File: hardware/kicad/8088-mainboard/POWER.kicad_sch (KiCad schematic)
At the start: 4 parts, among them J2 POWER 5v

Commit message: Add PSB board design
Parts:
- renumbered J2 to J1
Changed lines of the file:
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@@
 		(dnp no)
 		(fields_autoplaced yes)
-		(property "Reference" "J2"
+		(property "Reference" "J1"
 			(at 105.41 82.5499 90)
 			(show_name no)
@@
 			(project "8088-mainboard"
 				(path "/15ce4f45-6f32-456e-874c-aac11293789a/e9d836d6-3c3a-4b6e-a562-389c64894272"
-					(reference "J2")
+					(reference "J1")
 					(unit 1)
 				)

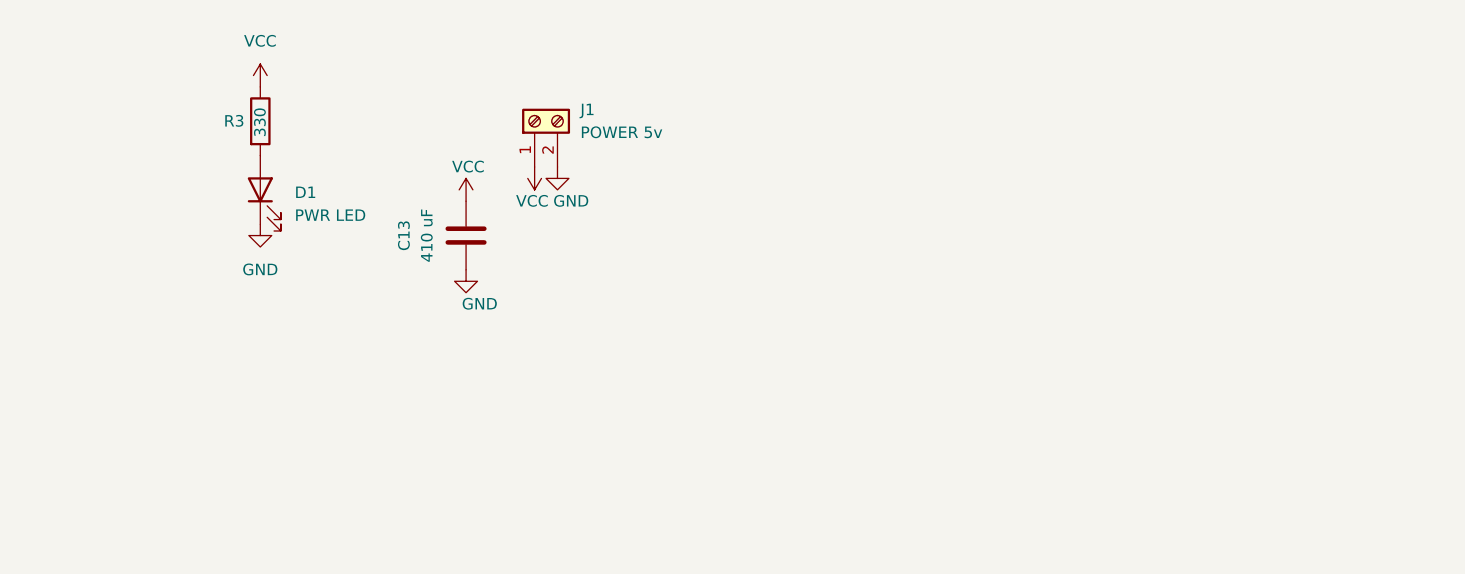
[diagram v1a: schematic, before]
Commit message: Update 8088-mainboard schematics for refined connections and label adjustments
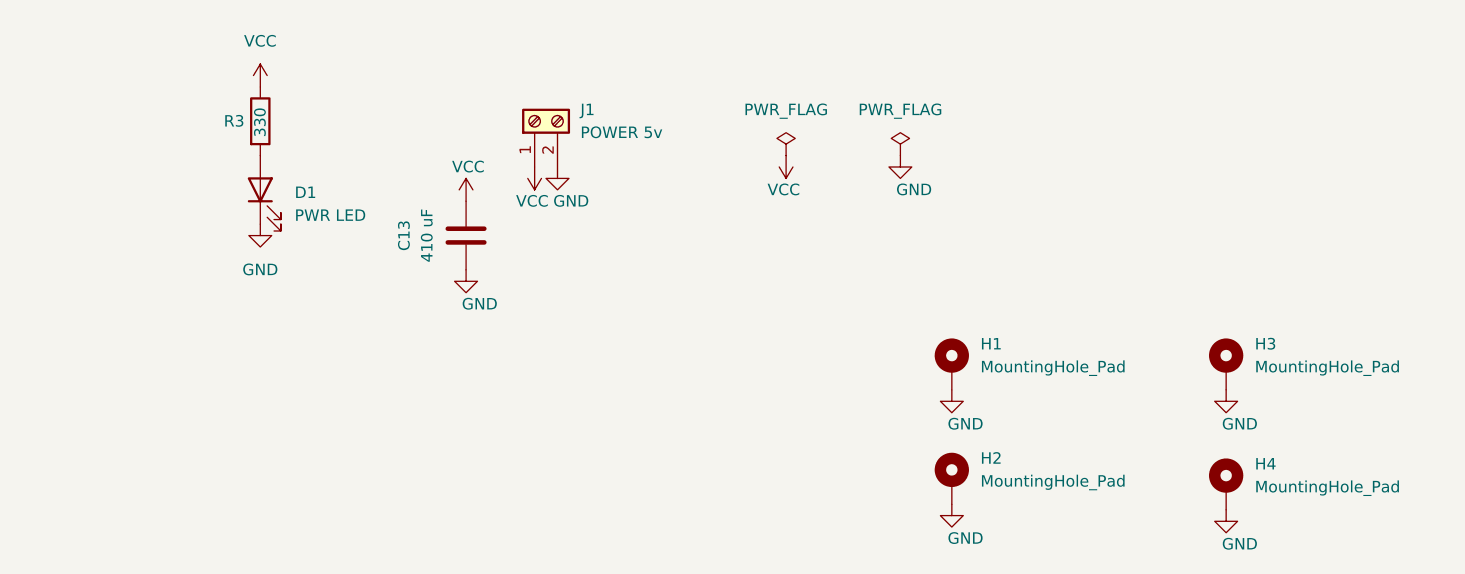
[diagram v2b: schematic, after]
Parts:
- added H1, H2, H3, H4: MountingHole_Pad, MountingHole:MountingHole_3.2mm_M3_Pad, symbol Mechanical:MountingHole_Pad
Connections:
- net GND: now also H1.1, H2.1, H3.1, H4.1

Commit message: Update 8086-mainboard scheme
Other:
- moved on the sheet: H1, H2, H3, H4
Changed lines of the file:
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@@
 	(symbol
 		(lib_id "power:GND")
-		(at 146.685 126.365 0)
+		(at 147.32 127 0)
 		(unit 1)
 		(body_style 1)
@@
 		(dnp no)
 		(property "Reference" "#PWR094"
-			(at 146.685 132.715 0)
+			(at 147.32 133.35 0)
 			(hide yes)
 			(show_name no)
@@
 		)
 		(property "Value" "GND"
-			(at 148.209 130.175 0)
+			(at 148.844 130.81 0)
 			(show_name no)
 			(do_not_autoplace no)
@@
 		)
 		(property "Footprint" ""
-			(at 146.685 126.365 0)
-			(hide yes)
-			(show_name no)
-			(do_not_autoplace no)
-			(effects
-				(font
-					(size 1.27 1.27)
-				)
-			)
-		)
-		(property "Datasheet" ""
-			(at 146.685 126.365 0)
+			(at 147.32 127 0)
+			(hide yes)
+			(show_name no)
+			(do_not_autoplace no)
+			(effects
+				(font
+					(size 1.27 1.27)
+				)
+			)
+		)
+		(property "Datasheet" ""
+			(at 147.32 127 0)
 			(hide yes)
 			(show_name no)
@@
 		)
 		(property "Description" "Power symbol creates a global label with name \"GND\" , ground"
-			(at 146.685 126.365 0)
+			(at 147.32 127 0)
 			(hide yes)
 			(show_name no)
@@
 	(symbol
 		(lib_id "Mechanical:MountingHole_Pad")
-		(at 146.685 111.125 0)
+		(at 147.32 111.76 0)
 		(unit 1)
 		(body_style 1)
@@
 		(fields_autoplaced yes)
 		(property "Reference" "H1"
-			(at 149.86 108.5849 0)
+			(at 150.495 109.2199 0)
 			(show_name no)
 			(do_not_autoplace no)
@@
 		)
 		(property "Value" "MountingHole_Pad"
-			(at 149.86 111.1249 0)
+			(at 150.495 111.7599 0)
 			(show_name no)
 			(do_not_autoplace no)
@@
 		)
 		(property "Footprint" "MountingHole:MountingHole_3.2mm_M3_Pad"
-			(at 146.685 111.125 0)
-			(hide yes)
-			(show_name no)
-			(do_not_autoplace no)
-			(effects
-				(font
-					(size 1.27 1.27)
-				)
-			)
-		)
-		(property "Datasheet" ""
-			(at 146.685 111.125 0)
+			(at 147.32 111.76 0)
+			(hide yes)
+			(show_name no)
+			(do_not_autoplace no)
+			(effects
+				(font
+					(size 1.27 1.27)
+				)
+			)
+		)
+		(property "Datasheet" ""
+			(at 147.32 111.76 0)
 			(hide yes)
 			(show_name no)
@@
 		)
 		(property "Description" "Mounting Hole with connection"
-			(at 146.685 111.125 0)
+			(at 147.32 111.76 0)
 			(hide yes)
 			(show_name no)
@@
 	(symbol
 		(lib_id "power:GND")
-		(at 146.685 113.665 0)
+		(at 147.32 114.3 0)
 		(unit 1)
 		(body_style 1)
@@
 		(dnp no)
 		(property "Reference" "#PWR093"
-			(at 146.685 120.015 0)
+			(at 147.32 120.65 0)
 			(hide yes)
 			(show_name no)
@@
 		)
 		(property "Value" "GND"
-			(at 148.209 117.475 0)
+			(at 148.844 118.11 0)
 			(show_name no)
 			(do_not_autoplace no)
@@
 		)
 		(property "Footprint" ""
-			(at 146.685 113.665 0)
-			(hide yes)
-			(show_name no)
-			(do_not_autoplace no)
-			(effects
-				(font
-					(size 1.27 1.27)
-				)
-			)
-		)
-		(property "Datasheet" ""
-			(at 146.685 113.665 0)
+			(at 147.32 114.3 0)
+			(hide yes)
+			(show_name no)
+			(do_not_autoplace no)
+			(effects
+				(font
+					(size 1.27 1.27)
+				)
+			)
+		)
+		(property "Datasheet" ""
+			(at 147.32 114.3 0)
 			(hide yes)
 			(show_name no)
@@
 		)
 		(property "Description" "Power symbol creates a global label with name \"GND\" , ground"
-			(at 146.685 113.665 0)
+			(at 147.32 114.3 0)
 			(hide yes)
 			(show_name no)
@@
 	(symbol
 		(lib_id "Mechanical:MountingHole_Pad")
-		(at 177.165 111.125 0)
+		(at 177.8 111.76 0)
 		(unit 1)
 		(body_style 1)
@@
 		(fields_autoplaced yes)
 		(property "Reference" "H3"
-			(at 180.34 108.5849 0)
+			(at 180.975 109.2199 0)
 			(show_name no)
 			(do_not_autoplace no)
@@
 		)
 		(property "Value" "MountingHole_Pad"
-			(at 180.34 111.1249 0)
+			(at 180.975 111.7599 0)
 			(show_name no)
 			(do_not_autoplace no)
@@
 		)
 		(property "Footprint" "MountingHole:MountingHole_3.2mm_M3_Pad"
-			(at 177.165 111.125 0)
-			(hide yes)
-			(show_name no)
-			(do_not_autoplace no)
-			(effects
-				(font
-					(size 1.27 1.27)
-				)
-			)
-		)
-		(property "Datasheet" ""
-			(at 177.165 111.125 0)
+			(at 177.8 111.76 0)
+			(hide yes)
+			(show_name no)
+			(do_not_autoplace no)
+			(effects
+				(font
+					(size 1.27 1.27)
+				)
+			)
+		)
+		(property "Datasheet" ""
+			(at 177.8 111.76 0)
 			(hide yes)
 			(show_name no)
@@
 		)
 		(property "Description" "Mounting Hole with connection"
-			(at 177.165 111.125 0)
+			(at 177.8 111.76 0)
 			(hide yes)
 			(show_name no)
@@
 	(symbol
 		(lib_id "power:GND")
-		(at 177.165 113.665 0)
+		(at 177.8 114.3 0)
 		(unit 1)
 		(body_style 1)
@@
 		(dnp no)
 		(property "Reference" "#PWR095"
-			(at 177.165 120.015 0)
+			(at 177.8 120.65 0)
 			(hide yes)
 			(show_name no)
@@
 		)
 		(property "Value" "GND"
-			(at 178.689 117.475 0)
+			(at 179.324 118.11 0)
 			(show_name no)
 			(do_not_autoplace no)
@@
 		)
 		(property "Footprint" ""
-			(at 177.165 113.665 0)
-			(hide yes)
-			(show_name no)
-			(do_not_autoplace no)
-			(effects
-				(font
-					(size 1.27 1.27)
-				)
-			)
-		)
-		(property "Datasheet" ""
-			(at 177.165 113.665 0)
+			(at 177.8 114.3 0)
+			(hide yes)
+			(show_name no)
+			(do_not_autoplace no)
+			(effects
+				(font
+					(size 1.27 1.27)
+				)
+			)
+		)
+		(property "Datasheet" ""
+			(at 177.8 114.3 0)
 			(hide yes)
 			(show_name no)
@@
 		)
 		(property "Description" "Power symbol creates a global label with name \"GND\" , ground"
-			(at 177.165 113.665 0)
+			(at 177.8 114.3 0)
 			(hide yes)
 			(show_name no)
@@
 	(symbol
 		(lib_id "power:GND")
-		(at 177.165 127 0)
+		(at 177.8 127 0)
 		(unit 1)
 		(body_style 1)
@@
 		(dnp no)
 		(property "Reference" "#PWR096"
-			(at 177.165 133.35 0)
+			(at 177.8 133.35 0)
 			(hide yes)
 			(show_name no)
@@
 		)
 		(property "Value" "GND"
-			(at 178.689 130.81 0)
+			(at 179.324 130.81 0)
 			(show_name no)
 			(do_not_autoplace no)
@@
 		)
 		(property "Footprint" ""
-			(at 177.165 127 0)
-			(hide yes)
-			(show_name no)
-			(do_not_autoplace no)
-			(effects
-				(font
-					(size 1.27 1.27)
-				)
-			)
-		)
-		(property "Datasheet" ""
-			(at 177.165 127 0)
+			(at 177.8 127 0)
+			(hide yes)
+			(show_name no)
+			(do_not_autoplace no)
+			(effects
+				(font
+					(size 1.27 1.27)
+				)
+			)
+		)
+		(property "Datasheet" ""
+			(at 177.8 127 0)
 			(hide yes)
 			(show_name no)
@@
 		)
 		(property "Description" "Power symbol creates a global label with name \"GND\" , ground"
-			(at 177.165 127 0)
+			(at 177.8 127 0)
 			(hide yes)
 			(show_name no)
@@
 	(symbol
 		(lib_id "Mechanical:MountingHole_Pad")
-		(at 177.165 124.46 0)
+		(at 177.8 124.46 0)
 		(unit 1)
 		(body_style 1)
@@
 		(fields_autoplaced yes)
 		(property "Reference" "H4"
-			(at 180.34 121.9199 0)
+			(at 180.975 121.9199 0)
 			(show_name no)
 			(do_not_autoplace no)
@@
 		)
 		(property "Value" "MountingHole_Pad"
-			(at 180.34 124.4599 0)
+			(at 180.975 124.4599 0)
 			(show_name no)
 			(do_not_autoplace no)
@@
 		)
 		(property "Footprint" "MountingHole:MountingHole_3.2mm_M3_Pad"
-			(at 177.165 124.46 0)
-			(hide yes)
-			(show_name no)
-			(do_not_autoplace no)
-			(effects
-				(font
-					(size 1.27 1.27)
-				)
-			)
-		)
-		(property "Datasheet" ""
-			(at 177.165 124.46 0)
+			(at 177.8 124.46 0)
+			(hide yes)
+			(show_name no)
+			(do_not_autoplace no)
+			(effects
+				(font
+					(size 1.27 1.27)
+				)
+			)
+		)
+		(property "Datasheet" ""
+			(at 177.8 124.46 0)
 			(hide yes)
 			(show_name no)
@@
 		)
 		(property "Description" "Mounting Hole with connection"
-			(at 177.165 124.46 0)
+			(at 177.8 124.46 0)
 			(hide yes)
 			(show_name no)
@@
 	(symbol
 		(lib_id "Mechanical:MountingHole_Pad")
-		(at 146.685 123.825 0)
+		(at 147.32 124.46 0)
 		(unit 1)
 		(body_style 1)
@@
 		(fields_autoplaced yes)
 		(property "Reference" "H2"
-			(at 149.86 121.2849 0)
+			(at 150.495 121.9199 0)
 			(show_name no)
 			(do_not_autoplace no)
@@
 		)
 		(property "Value" "MountingHole_Pad"
-			(at 149.86 123.8249 0)
+			(at 150.495 124.4599 0)
 			(show_name no)
 			(do_not_autoplace no)
@@
 		)
 		(property "Footprint" "MountingHole:MountingHole_3.2mm_M3_Pad"
-			(at 146.685 123.825 0)
-			(hide yes)
-			(show_name no)
-			(do_not_autoplace no)
-			(effects
-				(font
-					(size 1.27 1.27)
-				)
-			)
-		)
-		(property "Datasheet" ""
-			(at 146.685 123.825 0)
+			(at 147.32 124.46 0)
+			(hide yes)
+			(show_name no)
+			(do_not_autoplace no)
+			(effects
+				(font
+					(size 1.27 1.27)
+				)
+			)
+		)
+		(property "Datasheet" ""
+			(at 147.32 124.46 0)
 			(hide yes)
 			(show_name no)
@@
 		)
 		(property "Description" "Mounting Hole with connection"
-			(at 146.685 123.825 0)
-			(hide yes)
-			(show_name no)
+			(at 147.32 124.46 0)
+			(hide yes)
+			(show_name no)

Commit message: Finalize 8088 mainboard rev1.0 for production
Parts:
- added Q1: NDP6020P, Package_TO_SOT_THT:TO-220-3_Horizontal_TabDown, symbol Transistor_FET:Q_PMOS_GDS
- added R5: 10k, Resistor_THT:R_Axial_DIN0207_L6.3mm_D2.5mm_P7.62mm_Horizontal, symbol Device:R
- C13: value 410 uF -> 220 uF; footprint Capacitor_THT:CP_Radial_D8.0mm_P3.50mm -> Capacitor_THT:CP_Radial_D5.0mm_P2.00mm
- R4: renamed from R3; value 330 -> 2k
- renumbered J1 to J4
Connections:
- net GND: now also R5.2
- net VCC: now also Q1.3 (S); no longer J4.1 (Pin_1)
- new net: Q1.1 (G), R5.1
- new net: J4.1 (Pin_1), Q1.2 (D)
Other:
- moved on the sheet: C13, D1, R4
